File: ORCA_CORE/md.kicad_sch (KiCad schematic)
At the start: 23 parts, among them J12 Conn_01x02, J14 limit_sw_upper, J16 limit_sw_under, J21 Vin_motor, U3 AM2837, U5 TLP293, U7 AZ1117-3.3, U9 TLP293

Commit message: almost completed CORE
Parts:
- J13: renamed from J12; value Conn_01x02 -> md_out
- renumbered C1 to C3, C2 to C4, C5 to C6, C7 to C8, D1 to D2, H13 to H15, H14 to H16, J14 to J15, J16 to J20, J21 to J22, R10 to R11, R12 to R13, R14 to R15, R16 to R19, R17 to R20, R18 to R21, R22 to R23, R24 to R25, U9 to U10, U3 to U4, U5 to U6, U7 to U8
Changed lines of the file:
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@@
 	)
 	(global_label "+3V3"
-		(shape input)
+		(shape output)
 		(at 132.08 29.21 0)
 		(fields_autoplaced yes)
@@
 		(dnp no)
 		(fields_autoplaced yes)
-		(property "Reference" "#PWR040"
+		(property "Reference" "#PWR041"
 			(at 151.13 107.95 0)
 			(effects
@@
 		(dnp no)
 		(fields_autoplaced yes)
-		(property "Reference" "C1"
+		(property "Reference" "C3"
 			(at 104.14 44.45 0)
 			(effects
@@
 		(dnp no)
 		(fields_autoplaced yes)
-		(property "Reference" "R14"
+		(property "Reference" "R15"
 			(at 104.14 90.1699 0)
 			(effects
@@
 		(dnp no)
 		(fields_autoplaced yes)
-		(property "Reference" "#PWR042"
+		(property "Reference" "#PWR043"
 			(at 99.06 128.27 0)
 			(effects
@@
 		(dnp no)
 		(fields_autoplaced yes)
-		(property "Reference" "R22"
+		(property "Reference" "R23"
 			(at 186.69 35.5599 0)
 			(effects
@@
 		(on_board yes)
 		(dnp no)
-		(property "Reference" "U7"
+		(property "Reference" "U8"
 			(at 118.745 45.72 0)
 			(effects
@@
 		(dnp no)
 		(fields_autoplaced yes)
-		(property "Reference" "R16"
+		(property "Reference" "R19"
 			(at 95.25 116.84 90)
 			(effects
@@
 		(dnp no)
 		(fields_autoplaced yes)
-		(property "Reference" "#PWR046"
+		(property "Reference" "#PWR047"
 			(at 189.23 46.99 0)
 			(effects
@@
 		(dnp no)
 		(fields_autoplaced yes)
-		(property "Reference" "J12"
+		(property "Reference" "J13"
 			(at 190.5 105.4099 0)
 			(effects
@@
 			)
 		)
-		(property "Value" "Conn_01x02"
+		(property "Value" "md_out"
 			(at 190.5 107.9499 0)
 			(effects
@@
 		(dnp no)
 		(fields_autoplaced yes)
-		(property "Reference" "#PWR048"
+		(property "Reference" "#PWR049"
 			(at 250.19 46.99 0)
 			(effects
@@
 		(dnp no)
 		(fields_autoplaced yes)
-		(property "Reference" "#PWR026"
+		(property "Reference" "#PWR035"
 			(at 72.39 29.21 0)
 			(effects
@@
 		(dnp no)
 		(fields_autoplaced yes)
-		(property "Reference" "#FLG02"
+		(property "Reference" "#FLG03"
 			(at 192.405 171.45 0)
 			(effects
@@
 		(dnp no)
 		(fields_autoplaced yes)
-		(property "Reference" "J16"
+		(property "Reference" "J20"
 			(at 234.95 38.1 0)
 			(effects
@@
 		(dnp no)
 		(fields_autoplaced yes)
-		(property "Reference" "#PWR038"
+		(property "Reference" "#PWR039"
 			(at 99.06 102.87 0)
 			(effects
@@
 		(dnp no)
 		(fields_autoplaced yes)
-		(property "Reference" "H13"
+		(property "Reference" "H15"
 			(at 240.03 168.9099 0)
 			(effects
@@
 		(on_board yes)
 		(dnp no)
-		(property "Reference" "C5"
+		(property "Reference" "C6"
 			(at 164.084 115.062 90)
 			(effects
@@
 		(dnp no)
 		(fields_autoplaced yes)
-		(property "Reference" "J14"
+		(property "Reference" "J15"
 			(at 173.99 38.1 0)
 			(effects
@@
 		(on_board yes)
 		(dnp no)
-		(property "Reference" "C7"
+		(property "Reference" "C8"
 			(at 164.084 121.412 90)
 			(effects
@@
 		(dnp no)
 		(fields_autoplaced yes)
-		(property "Reference" "#PWR050"
+		(property "Reference" "#PWR051"
 			(at 167.64 138.43 0)
 			(effects
@@
 		(dnp no)
 		(fields_autoplaced yes)
-		(property "Reference" "R24"
+		(property "Reference" "R25"
 			(at 247.65 35.5599 0)
 			(effects
@@
 		(dnp no)
 		(fields_autoplaced yes)
-		(property "Reference" "R10"
+		(property "Reference" "R11"
 			(at 95.25 91.44 90)
 			(effects
@@
 		(dnp no)
 		(fields_autoplaced yes)
-		(property "Reference" "H14"
+		(property "Reference" "H16"
 			(at 240.03 176.5299 0)
 			(effects
@@
 		(dnp no)
 		(fields_autoplaced yes)
-		(property "Reference" "D1"
+		(property "Reference" "D2"
 			(at 115.2525 26.67 0)
 			(effects
@@
 		(dnp no)
 		(fields_autoplaced yes)
-		(property "Reference" "J21"
+		(property "Reference" "J22"
 			(at 30.48 46.99 0)
 			(effects
@@
 		(dnp no)
 		(fields_autoplaced yes)
-		(property "Reference" "C2"
+		(property "Reference" "C4"
 			(at 133.985 44.45 0)
 			(effects
@@
 		(dnp no)
 		(fields_autoplaced yes)
-		(property "Reference" "R17"
+		(property "Reference" "R20"
 			(at 104.14 115.5699 0)
 			(effects
@@
 		(dnp no)
 		(fields_autoplaced yes)
-		(property "Reference" "U3"
+		(property "Reference" "U4"
 			(at 166.37 96.52 0)
 			(effects
@@
 		(dnp no)
 		(fields_autoplaced yes)
-		(property "Reference" "#PWR044"
+		(property "Reference" "#PWR045"
 			(at 115.57 58.42 0)
 			(effects
@@
 		(dnp no)
 		(fields_autoplaced yes)
-		(property "Reference" "#PWR052"
+		(property "Reference" "#PWR053"
 			(at 41.91 55.88 0)
 			(effects
@@
 		(dnp no)
 		(fields_autoplaced yes)
-		(property "Reference" "U9"
+		(property "Reference" "U10"
 			(at 113.03 116.84 0)
 			(effects
@@
 		(dnp no)
 		(fields_autoplaced yes)
-		(property "Reference" "#FLG04"
+		(property "Reference" "#FLG05"
 			(at 192.405 175.26 0)
 			(effects
@@
 		(dnp no)
 		(fields_autoplaced yes)
-		(property "Reference" "#PWR036"
+		(property "Reference" "#PWR037"
 			(at 72.39 25.4 0)
 			(effects
@@
 		(dnp no)
 		(fields_autoplaced yes)
-		(property "Reference" "R18"
+		(property "Reference" "R21"
 			(at 124.46 116.84 90)
 			(effects
@@
 		(dnp no)
 		(fields_autoplaced yes)
-		(property "Reference" "U5"
+		(property "Reference" "U6"
 			(at 113.03 91.44 0)
 			(effects
@@
 		(dnp no)
 		(fields_autoplaced yes)
-		(property "Reference" "R12"
+		(property "Reference" "R13"
 			(at 124.46 91.44 90)
 			(effects

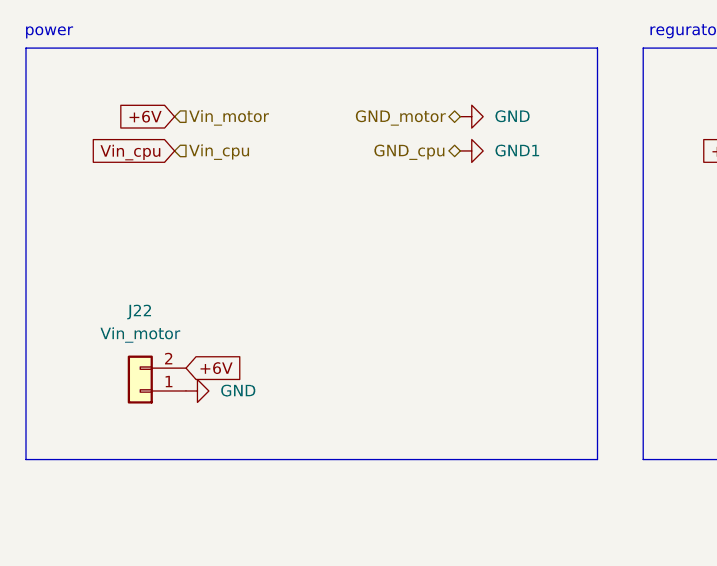
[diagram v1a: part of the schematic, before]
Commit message: complete attaching footprint of CORE
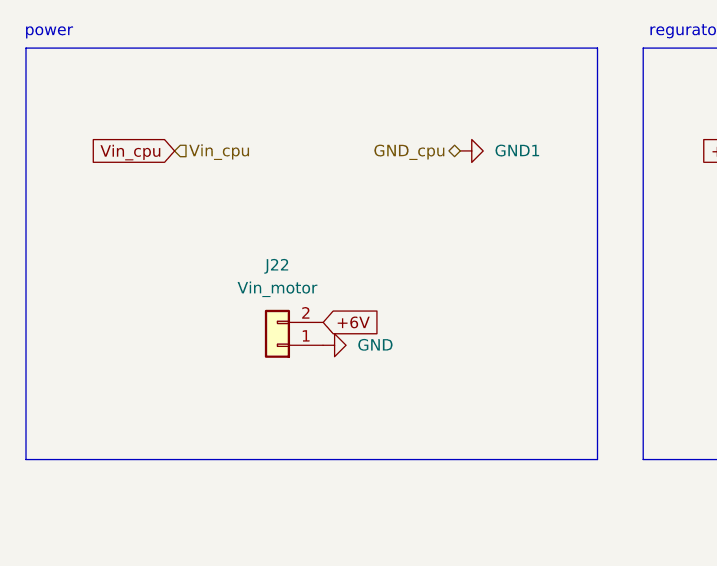
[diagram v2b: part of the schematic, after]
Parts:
- C6: footprint (none) -> Capacitor_SMD:C_0603_1608Metric_Pad1.08x0.95mm_HandSolder
- C8: footprint (none) -> Capacitor_SMD:C_1206_3216Metric_Pad1.33x1.80mm_HandSolder
- R11, R13, R15, R19, R20, R21, R23, R25: footprint (none) -> Resistor_SMD:R_0603_1608Metric_Pad0.98x0.95mm_HandSolder
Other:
- moved on the sheet: J22
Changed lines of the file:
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@@
 	(global_label "+6V"
 		(shape input)
-		(at 34.29 25.4 180)
+		(at 50.8 48.26 0)
 		(fields_autoplaced yes)
 		(effects
@@
 				(size 1.27 1.27)
 			)
-			(justify right)
+			(justify left)
 		)
 		(property "Intersheetrefs" "${INTERSHEET_REFS}"
-			(at 27.4343 25.4 0)
-			(effects
-				(font
-					(size 1.27 1.27)
-				)
-				(justify right)
-				(hide yes)
-			)
-		)
-	)
-	(global_label "+6V"
+			(at 57.6557 48.26 0)
+			(effects
+				(font
+					(size 1.27 1.27)
+				)
+				(justify left)
+				(hide yes)
+			)
+		)
+	)
+	(global_label "+3V3"
 		(shape input)
-		(at 35.56 53.34 0)
+		(at 128.27 123.19 0)
 		(fields_autoplaced yes)
 		(effects
@@
 		)
 		(property "Intersheetrefs" "${INTERSHEET_REFS}"
-			(at 42.4157 53.34 0)
+			(at 136.3352 123.19 0)
 			(effects
 				(font
@@
 	)
 	(global_label "+3V3"
-		(shape input)
-		(at 128.27 123.19 0)
+		(shape output)
+		(at 132.08 29.21 0)
 		(fields_autoplaced yes)
 		(effects
@@
 		)
 		(property "Intersheetrefs" "${INTERSHEET_REFS}"
-			(at 136.3352 123.19 0)
+			(at 140.1452 29.21 0)
 			(effects
 				(font
@@
 		)
 	)
-	(global_label "+3V3"
+	(hierarchical_label "limit_sw_upper"
 		(shape output)
-		(at 132.08 29.21 0)
+		(at 195.58 44.45 0)
 		(fields_autoplaced yes)
 		(effects
@@
 			(justify left)
 		)
-		(property "Intersheetrefs" "${INTERSHEET_REFS}"
-			(at 140.1452 29.21 0)
-			(effects
-				(font
-					(size 1.27 1.27)
-				)
-				(justify left)
-				(hide yes)
-			)
-		)
-	)
-	(hierarchical_label "limit_sw_upper"
-		(shape output)
-		(at 195.58 44.45 0)
+	)
+	(hierarchical_label "Vin_cpu"
+		(shape input)
+		(at 34.29 29.21 0)
 		(fields_autoplaced yes)
 		(effects
@@
 		)
 	)
-	(hierarchical_label "Vin_cpu"
-		(shape input)
-		(at 34.29 29.21 0)
+	(hierarchical_label "GND_cpu"
+		(shape bidirectional)
+		(at 66.04 29.21 180)
 		(fields_autoplaced yes)
 		(effects
@@
 				(size 1.27 1.27)
 			)
-			(justify left)
-		)
-	)
-	(hierarchical_label "GND_motor"
-		(shape bidirectional)
-		(at 66.04 25.4 180)
+			(justify right)
+		)
+	)
+	(hierarchical_label "limit_sw_under"
+		(shape output)
+		(at 256.54 44.45 0)
 		(fields_autoplaced yes)
 		(effects
@@
 				(size 1.27 1.27)
 			)
-			(justify right)
-		)
-	)
-	(hierarchical_label "GND_cpu"
+			(justify left)
+		)
+	)
+	(hierarchical_label "IN_B"
 		(shape bidirectional)
-		(at 66.04 29.21 180)
+		(at 91.44 123.19 180)
 		(fields_autoplaced yes)
 		(effects
@@
 		)
 	)
-	(hierarchical_label "limit_sw_under"
-		(shape output)
-		(at 256.54 44.45 0)
+	(hierarchical_label "IN_A"
+		(shape bidirectional)
+		(at 91.44 97.79 180)
 		(fields_autoplaced yes)
 		(effects
@@
 				(size 1.27 1.27)
 			)
-			(justify left)
-		)
-	)
-	(hierarchical_label "IN_B"
-		(shape bidirectional)
-		(at 91.44 123.19 180)
-		(fields_autoplaced yes)
-		(effects
-			(font
-				(size 1.27 1.27)
-			)
 			(justify right)
-		)
-	)
-	(hierarchical_label "IN_A"
-		(shape bidirectional)
-		(at 91.44 97.79 180)
-		(fields_autoplaced yes)
-		(effects
-			(font
-				(size 1.27 1.27)
-			)
-			(justify right)
-		)
-	)
-	(hierarchical_label "Vin_motor"
-		(shape input)
-		(at 34.29 25.4 0)
-		(fields_autoplaced yes)
-		(effects
-			(font
-				(size 1.27 1.27)
-			)
-			(justify left)
 		)
 	)
@@
 			)
 		)
-		(property "Footprint" ""
+		(property "Footprint" "Resistor_SMD:R_0603_1608Metric_Pad0.98x0.95mm_HandSolder"
 			(at 103.378 91.44 90)
 			(effects
@@
 			)
 		)
-		(property "Footprint" ""
+		(property "Footprint" "Resistor_SMD:R_0603_1608Metric_Pad0.98x0.95mm_HandSolder"
 			(at 182.372 36.83 90)
 			(effects
@@
 			)
 		)
-		(property "Footprint" ""
+		(property "Footprint" "Resistor_SMD:R_0603_1608Metric_Pad0.98x0.95mm_HandSolder"
 			(at 95.25 124.968 90)
 			(effects
@@
 			)
 		)
-		(property "Footprint" ""
+		(property "Footprint" "Capacitor_SMD:C_0603_1608Metric_Pad1.08x0.95mm_HandSolder"
 			(at 163.83 118.4148 0)
 			(effects
@@
 			)
 		)
-		(property "Footprint" ""
+		(property "Footprint" "Capacitor_SMD:C_1206_3216Metric_Pad1.33x1.80mm_HandSolder"
 			(at 163.83 124.7648 0)
 			(effects
@@
 			)
 		)
-		(property "Footprint" ""
+		(property "Footprint" "Resistor_SMD:R_0603_1608Metric_Pad0.98x0.95mm_HandSolder"
 			(at 243.332 36.83 90)
 			(effects
@@
 			)
 		)
-		(property "Footprint" ""
+		(property "Footprint" "Resistor_SMD:R_0603_1608Metric_Pad0.98x0.95mm_HandSolder"
 			(at 95.25 99.568 90)
 			(effects
@@
 	(symbol
 		(lib_id "Connector_Generic:Conn_01x02")
-		(at 30.48 55.88 180)
+		(at 45.72 50.8 180)
 		(unit 1)
 		(exclude_from_sim no)
@@
 		(fields_autoplaced yes)
 		(property "Reference" "J22"
-			(at 30.48 46.99 0)
+			(at 45.72 41.91 0)
 			(effects
 				(font
@@
 		)
 		(property "Value" "Vin_motor"
-			(at 30.48 49.53 0)
+			(at 45.72 44.45 0)
 			(effects
 				(font
@@
 		)
 		(property "Footprint" "Connector_JST:JST_XH_S2B-XH-A_1x02_P2.50mm_Horizontal"
-			(at 30.48 55.88 0)
+			(at 45.72 50.8 0)
 			(effects
 				(font
@@
 		)
 		(property "Datasheet" "~"
-			(at 30.48 55.88 0)
+			(at 45.72 50.8 0)
 			(effects
 				(font
@@
 		)
 		(property "Description" "Generic connector, single row, 01x02, script generated (kicad-library-utils/schlib/autogen/connector/)"
-			(at 30.48 55.88 0)
+			(at 45.72 50.8 0)
 			(effects
 				(font
@@
 			)
 		)
-		(property "Footprint" ""
+		(property "Footprint" "Resistor_SMD:R_0603_1608Metric_Pad0.98x0.95mm_HandSolder"
 			(at 103.378 116.84 90)
 			(effects
@@
 	(symbol
 		(lib_id "power:GND")
-		(at 35.56 55.88 90)
+		(at 50.8 50.8 90)
 		(unit 1)
 		(exclude_from_sim no)
@@
 		(fields_autoplaced yes)
 		(property "Reference" "#PWR053"
-			(at 41.91 55.88 0)
+			(at 57.15 50.8 0)
 			(effects
 				(font
@@
 		)
 		(property "Value" "GND"
-			(at 39.37 55.8799 90)
+			(at 54.61 50.7999 90)
 			(effects
 				(font
@@
 		)
 		(property "Footprint" ""
-			(at 35.56 55.88 0)
+			(at 50.8 50.8 0)
 			(effects
 				(font
@@
 		)
 		(property "Datasheet" ""
-			(at 35.56 55.88 0)
+			(at 50.8 50.8 0)
 			(effects
 				(font
@@
 		)
 		(property "Description" "Power symbol creates a global label with name \"GND\" , ground"
-			(at 35.56 55.88 0)
+			(at 50.8 50.8 0)
 			(effects
 				(font
@@
 	)
 	(symbol
-		(lib_id "power:GND")
-		(at 66.04 25.4 90)
-		(unit 1)
-		(exclude_from_sim no)
-		(in_bom yes)
-		(on_board yes)
-		(dnp no)
-		(fields_autoplaced yes)
-		(property "Reference" "#PWR037"
-			(at 72.39 25.4 0)
-			(effects
-				(font
-					(size 1.27 1.27)
-				)
-				(hide yes)
-			)
-		)
-		(property "Value" "GND"
-			(at 69.85 25.3999 90)
-			(effects
-				(font
-					(size 1.27 1.27)
-				)
-				(justify right)
-			)
-		)
-		(property "Footprint" ""
-			(at 66.04 25.4 0)
-			(effects
-				(font
-					(size 1.27 1.27)
-				)
-				(hide yes)
-			)
-		)
-		(property "Datasheet" ""
-			(at 66.04 25.4 0)
-			(effects
-				(font
-					(size 1.27 1.27)
-				)
-				(hide yes)
-			)
-		)
-		(property "Description" "Power symbol creates a global label with name \"GND\" , ground"
-			(at 66.04 25.4 0)
-			(effects
-				(font
-					(size 1.27 1.27)
-				)
-				(hide yes)
-			)
-		)
-		(pin "1"
-		)
-		(instances
-			(project ""
-				(path "/895d6bb7-4008-488b-a34b-0077e9f7e4a1/880e87ff-23ea-4a52-b228-11eaa0fc1d65"
-					(reference "#PWR037")
-					(unit 1)
-				)
-				(path "/895d6bb7-4008-488b-a34b-0077e9f7e4a1/c77acf15-1268-4efe-b693-edffd64e020d"
-					(reference "#PWR036")
-					(unit 1)
-				)
-			)
-		)
-	)
-	(symbol
 		(lib_id "Device:R")
 		(at 124.46 123.19 90)
@@
 			)
 		)
-		(property "Footprint" ""
+		(property "Footprint" "Resistor_SMD:R_0603_1608Metric_Pad0.98x0.95mm_HandSolder"
 			(at 124.46 124.968 90)
 			(effects
@@
 			)
 		)
-		(property "Footprint" ""
+		(property "Footprint" "Resistor_SMD:R_0603_1608Metric_Pad0.98x0.95mm_HandSolder"
 			(at 124.46 99.568 90)
 			(effects

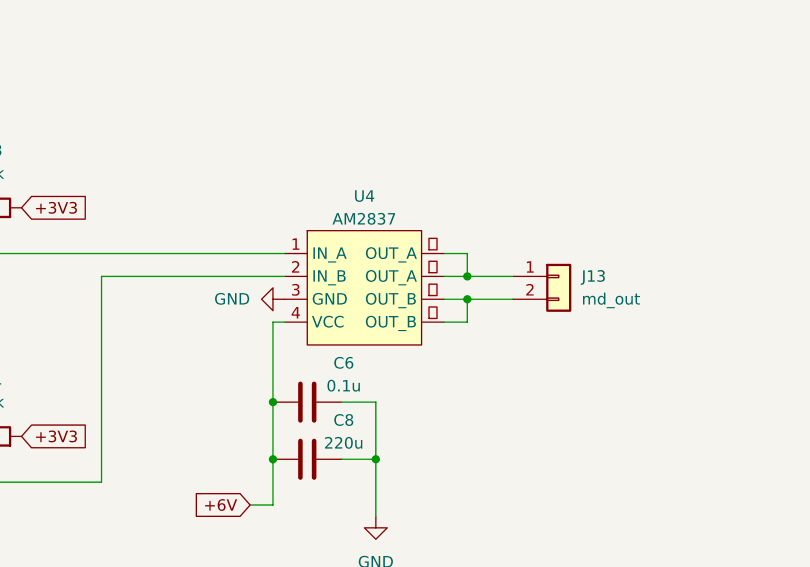
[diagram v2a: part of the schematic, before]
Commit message: made board outline and import it
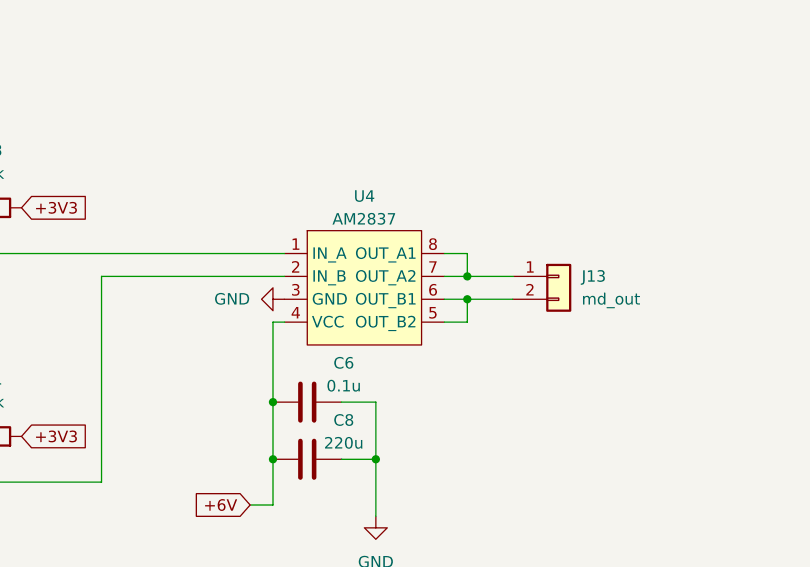
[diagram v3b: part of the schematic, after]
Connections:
- new net: J13.1 (Pin_1), U4.7 (OUT_A2), U4.8 (OUT_A1)
- new net: J13.2 (Pin_2), U4.5 (OUT_B2), U4.6 (OUT_B1)

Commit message: most of wire placed. try update kicad to use replicate library
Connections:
- net Vin_cpu: no longer R15.2, R20.2, R23.1, R25.1
- new net Vin_md: R15.2, R20.2, R23.1, R25.1
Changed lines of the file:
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@@
 		)
 	)
-	(global_label "Vin_cpu"
+	(global_label "Vin_md"
 		(shape input)
 		(at 181.61 30.48 180)
@@
 		)
 		(property "Intersheetrefs" "${INTERSHEET_REFS}"
-			(at 171.4282 30.48 0)
-			(effects
-				(font
-					(size 1.27 1.27)
-				)
-				(justify right)
-				(hide yes)
-			)
-		)
-	)
-	(global_label "Vin_cpu"
+			(at 171.9725 30.48 0)
+			(effects
+				(font
+					(size 1.27 1.27)
+				)
+				(justify right)
+				(hide yes)
+			)
+		)
+	)
+	(global_label "Vin_md"
 		(shape input)
 		(at 242.57 30.48 180)
@@
 		)
 		(property "Intersheetrefs" "${INTERSHEET_REFS}"
-			(at 232.3882 30.48 0)
-			(effects
-				(font
-					(size 1.27 1.27)
-				)
-				(justify right)
-				(hide yes)
-			)
-		)
-	)
-	(global_label "Vin_cpu"
+			(at 232.9325 30.48 0)
+			(effects
+				(font
+					(size 1.27 1.27)
+				)
+				(justify right)
+				(hide yes)
+			)
+		)
+	)
+	(global_label "Vin_md"
 		(shape input)
 		(at 34.29 29.21 180)
@@
 		)
 		(property "Intersheetrefs" "${INTERSHEET_REFS}"
-			(at 24.1082 29.21 0)
+			(at 24.6525 29.21 0)
 			(effects
 				(font
@@
 		)
 	)
-	(global_label "Vin_cpu"
+	(global_label "Vin_md"
 		(shape input)
 		(at 100.33 85.09 180)
@@
 		)
 		(property "Intersheetrefs" "${INTERSHEET_REFS}"
-			(at 90.1482 85.09 0)
+			(at 90.6925 85.09 0)
 			(effects
 				(font
@@
 		)
 	)
-	(global_label "Vin_cpu"
+	(global_label "Vin_md"
 		(shape input)
 		(at 100.33 110.49 180)
@@
 		)
 		(property "Intersheetrefs" "${INTERSHEET_REFS}"
-			(at 90.1482 110.49 0)
+			(at 90.6925 110.49 0)
 			(effects
 				(font
@@
 		)
 	)
-	(hierarchical_label "Vin_cpu"
+	(hierarchical_label "Vin_md"
 		(shape input)
 		(at 34.29 29.21 0)
